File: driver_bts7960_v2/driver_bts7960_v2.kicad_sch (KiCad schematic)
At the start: 27 parts, among them J1 Motor_1, J2 Alimentacion, J6 Motor_2, J7 Conn_02x04_Odd_Even, U1 BTS7960B, U2 BTS7960B, U3 BTS7960B, U4 BTS7960B

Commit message: v2
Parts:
- J1, J6: footprint Connector_AMASS:AMASS_XT30PW-M_1x02_P2.50mm_Horizontal -> Connector_AMASS:AMASS_XT30UPB-F_1x02_P5.0mm_Vertical
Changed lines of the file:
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@@
 			)
 		)
-		(property "Footprint" "Connector_AMASS:AMASS_XT30PW-M_1x02_P2.50mm_Horizontal"
+		(property "Footprint" "Connector_AMASS:AMASS_XT30UPB-F_1x02_P5.0mm_Vertical"
 			(at 205.74 43.18 0)
 			(effects
@@
 			)
 		)
-		(property "Footprint" "Connector_AMASS:AMASS_XT30PW-M_1x02_P2.50mm_Horizontal"
+		(property "Footprint" "Connector_AMASS:AMASS_XT30UPB-F_1x02_P5.0mm_Vertical"
 			(at 106.68 43.18 0)
 			(effects

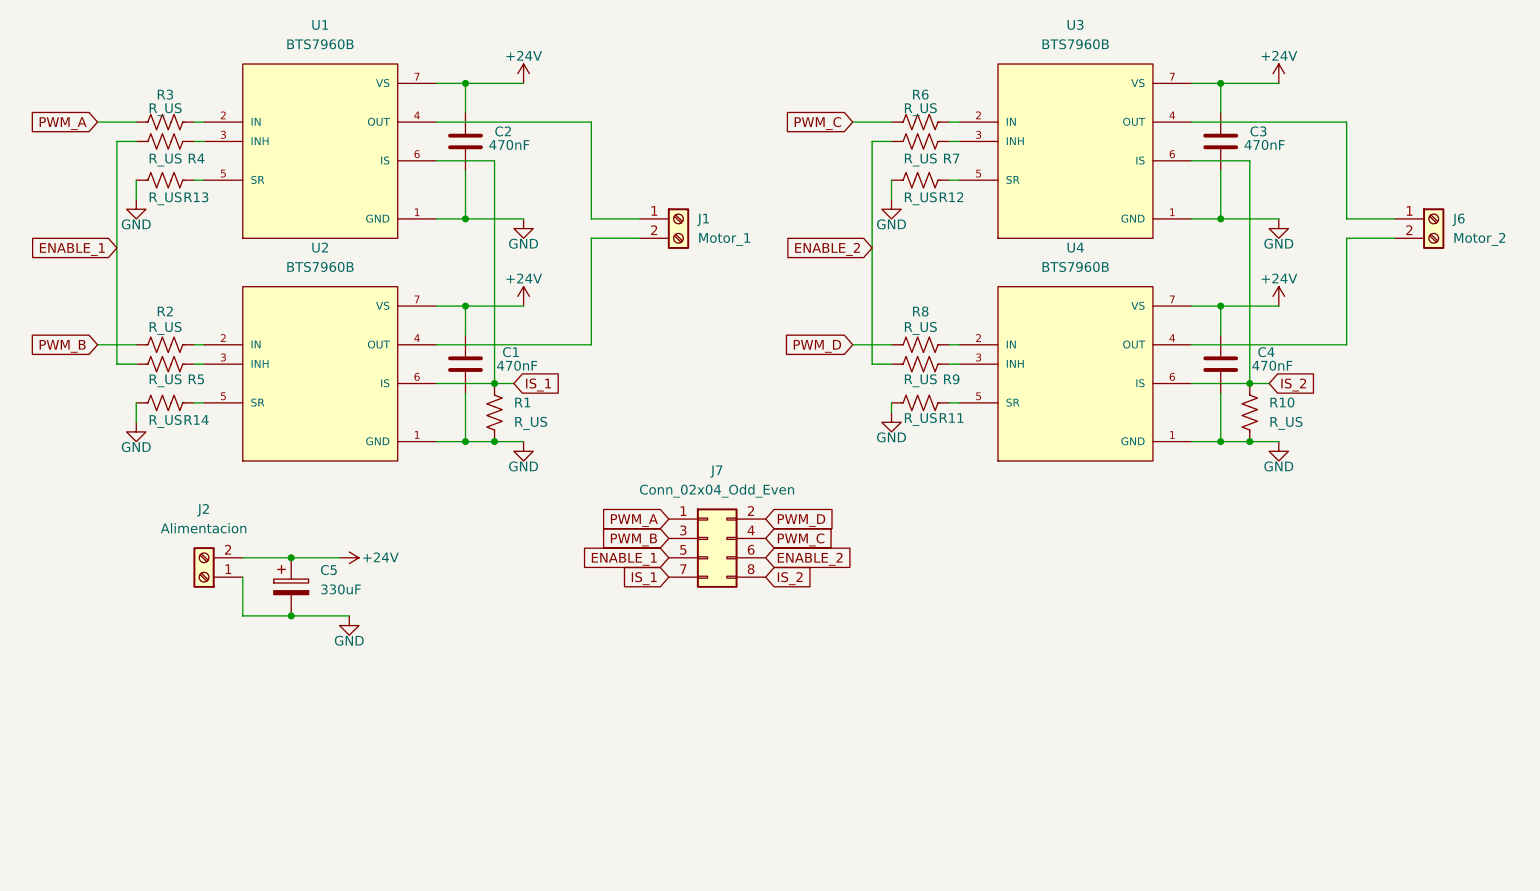
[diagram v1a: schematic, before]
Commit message: v2 terminado con 74hc244
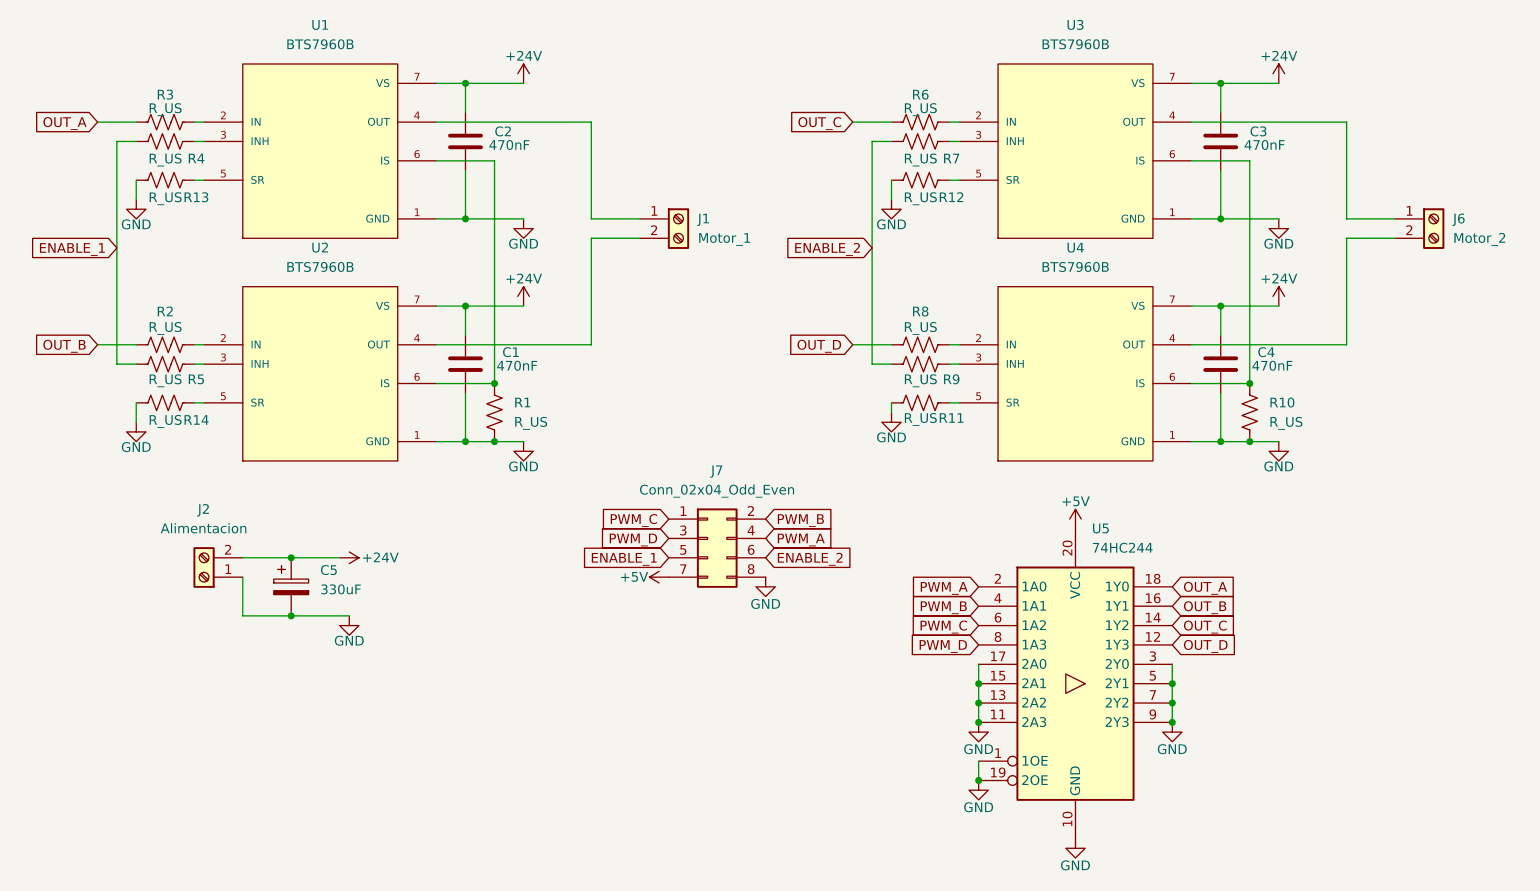
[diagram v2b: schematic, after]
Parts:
- added U5: 74HC244, Package_SO:SSOP-20_4.4x6.5mm_P0.65mm, symbol 74xx:74HC244
- J7: footprint Connector_PinHeader_2.54mm:PinHeader_2x04_P2.54mm_Horizontal -> Connector_PinHeader_2.54mm:PinHeader_2x04_P2.54mm_Vertical
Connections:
- net GND: now also J7.8 (Pin_8), U5.1 (1OE), U5.10 (GND), U5.11 (2A3), U5.13 (2A2), U5.15 (2A1), U5.17 (2A0), U5.19 (2OE), U5.3 (2Y0), U5.5 (2Y1), U5.7 (2Y2), U5.9 (2Y3)
- net PWM_A: now also J7.4 (Pin_4), U5.2 (1A0); no longer J7.1 (Pin_1), R3.2
- net PWM_B: now also J7.2 (Pin_2), U5.4 (1A1); no longer J7.3 (Pin_3), R2.2
- net PWM_C: now also J7.1 (Pin_1), U5.6 (1A2); no longer J7.4 (Pin_4), R6.2
- net PWM_D: now also J7.3 (Pin_3), U5.8 (1A3); no longer J7.2 (Pin_2), R8.2
- net IS_1: no longer names the net of R1.1, U1.6 (IS), U2.6 (IS)
- net IS_1: no longer J7.7 (Pin_7)
- net IS_2: no longer names the net of R10.1, U3.6 (IS), U4.6 (IS)
- net IS_2: no longer J7.8 (Pin_8)
- new net +5V: J7.7 (Pin_7), U5.20 (VCC)
- new net OUT_A: R3.2, U5.18 (1Y0)
- new net OUT_B: R2.2, U5.16 (1Y1)
- new net OUT_C: R6.2, U5.14 (1Y2)
- new net OUT_D: R8.2, U5.12 (1Y3)
